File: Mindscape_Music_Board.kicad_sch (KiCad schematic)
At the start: 12 parts, among them J1 Conn_02x31_Row_Letter_First, SW1 SW_DIP_x08, U1 74LS08, U2 74LS74, U3 LM386, U4 74LS04, U5 74LS08, U6 74LS85, U7 74LS85, U8 AY-3-8913, U9 AY-3-8913

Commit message: More routing/footprints.
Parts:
- added C1, C11, C12, C2, C4, C5, C7, C99: C, Capacitor_THT:C_Disc_D7.5mm_W5.0mm_P7.50mm, symbol Device:C
- added C10: 470uF/16V, Capacitor_THT:CP_Axial_L18.0mm_D8.0mm_P25.00mm_Horizontal, symbol Device:C_Polarized
- added C14, C15: ?, Capacitor_THT:CP_Radial_Tantal_D4.5mm_P5.00mm, symbol Device:C_Polarized
- added C3, C8, C98: ?, Capacitor_THT:CP_Radial_D5.0mm_P2.50mm, symbol Device:C_Polarized
- added C6: C, Capacitor_THT:C_Disc_D3.0mm_W1.6mm_P2.50mm, symbol Device:C
- added J2: AudioJack2, MMB_Library:Audio_Jack, symbol Connector_Audio:AudioJack2
- added R1: 10, Resistor_THT:R_Axial_DIN0309_L9.0mm_D3.2mm_P12.70mm_Horizontal, symbol Device:R
- added R2, R3: ?, Resistor_THT:R_Axial_DIN0309_L9.0mm_D3.2mm_P12.70mm_Horizontal, symbol Device:R
- added RV1: 10K?, MMB_Library:Potentiometer, symbol Device:R_Potentiometer
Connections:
- net +12V: now also U3.6 (V+), C14.1, C6.1
- net AEN: now also U4.5
- net ANALOG: now also R2.1, R3.1
- net CLK: now also U2.2 (D), U2.6 (~{Q})
- net GND: now also C1.2, C11.2, C12.2, C14.2, C15.2, C2.2, C3.2, C4.2, C5.2, C6.2, C7.2, C98.2, C99.2, J2.S, R3.2, RV1.3; no longer J1.b10 (Pin_b10), J1.b31 (Pin_b31)
- net ISA_CLK: now also U2.3 (C)
- net VCC: now also C1.1, C11.1, C12.1, C15.1, C2.1, C4.1, C5.1
- net ~{IOR}: now also U1.13
- net ~{IOW}: now also U4.11
- net ~{RESET}: now also C98.1
- net BDIR1: now reaches U5.8
- net BDIR1: now also U9.2 (BDIR)
- net ~{AEN}: now reaches U4.6
- net ~{AEN}: now also U6.3 (Ia=b)
- net BC1_1: now reaches U9.3 (BC1)
- net BC1_1: now also U5.11
- net BDIR0: now reaches U8.2 (BDIR)
- net BDIR0: now also U5.6
- net BC1_0: now reaches U8.3 (BC1)
- net BC1_0: now also U5.3
- net at U7.2 (Ia<b): now also U6.7 (Oa<b)
- net at U7.3 (Ia=b): now also U6.6 (Oa=b)
- net ADDR_MATCH: now reaches U7.6 (Oa=b)
- net at U1.10: now also U1.5
- net at U3.3 (+): now also RV1.2
- net at U3.5: now also C10.1, R1.1
- new net: C99.1, R1.2
- new net: C8.2, RV1.1
- new net: C7.1, C8.1, R2.2
- new net: C10.2, J2.T
- no-connect marks 1 -> 7
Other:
- note added: "(CHIP1)"
- note added: "(DATA)"
- note added: "(~{CHIP1})"
- note added: "(~{DATA})"
- note added: "Function of this FF is an (un)educated guess"
- moved on the sheet: J1, RN1, SW1, U1A, U1B, U1C, U1D, U1E, U2B, U2C, U3, U4A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

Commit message: Worked out glue/decoding (hopefully).
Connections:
- net A1: now also U1.4
- net ADDR_MATCH: now also U1.10, U1.5
- net BC1_0: now also U5.11, U9.3 (BC1); no longer U5.3, U8.3 (BC1)
- net BC1_1: now also U5.3, U8.3 (BC1); no longer U5.11, U9.3 (BC1)
- net BDIR0: now also U5.8, U9.2 (BDIR); no longer U5.6, U8.2 (BDIR)
- net BDIR1: now also U5.6, U8.2 (BDIR); no longer U5.8, U9.2 (BDIR)
- net CHIP0: now also U1.9, U4.8
- net CONTROL: now also U1.1, U4.12
- net at U1.11: now also U4.1
- net at U1.12: now also U4.4
- net at U4.10, U5.10, U5.5: now also U1.2
- net at U5.9: now also U1.8, U5.12
- net at C3.1: now also U3.7 (BYPASS)
- net at U5.4: now also U1.6, U5.2
- net at U4.3: now also U1.3
- net ~{AEN}: no longer names the net of U4.6, U6.3 (Ia=b)
- no-connect marks 7 -> 9
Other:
- moved on the sheet: C3, J1, U1A, U1B, U1C, U1D, U1E, U2A, U2B, U2C, U4A, U4B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

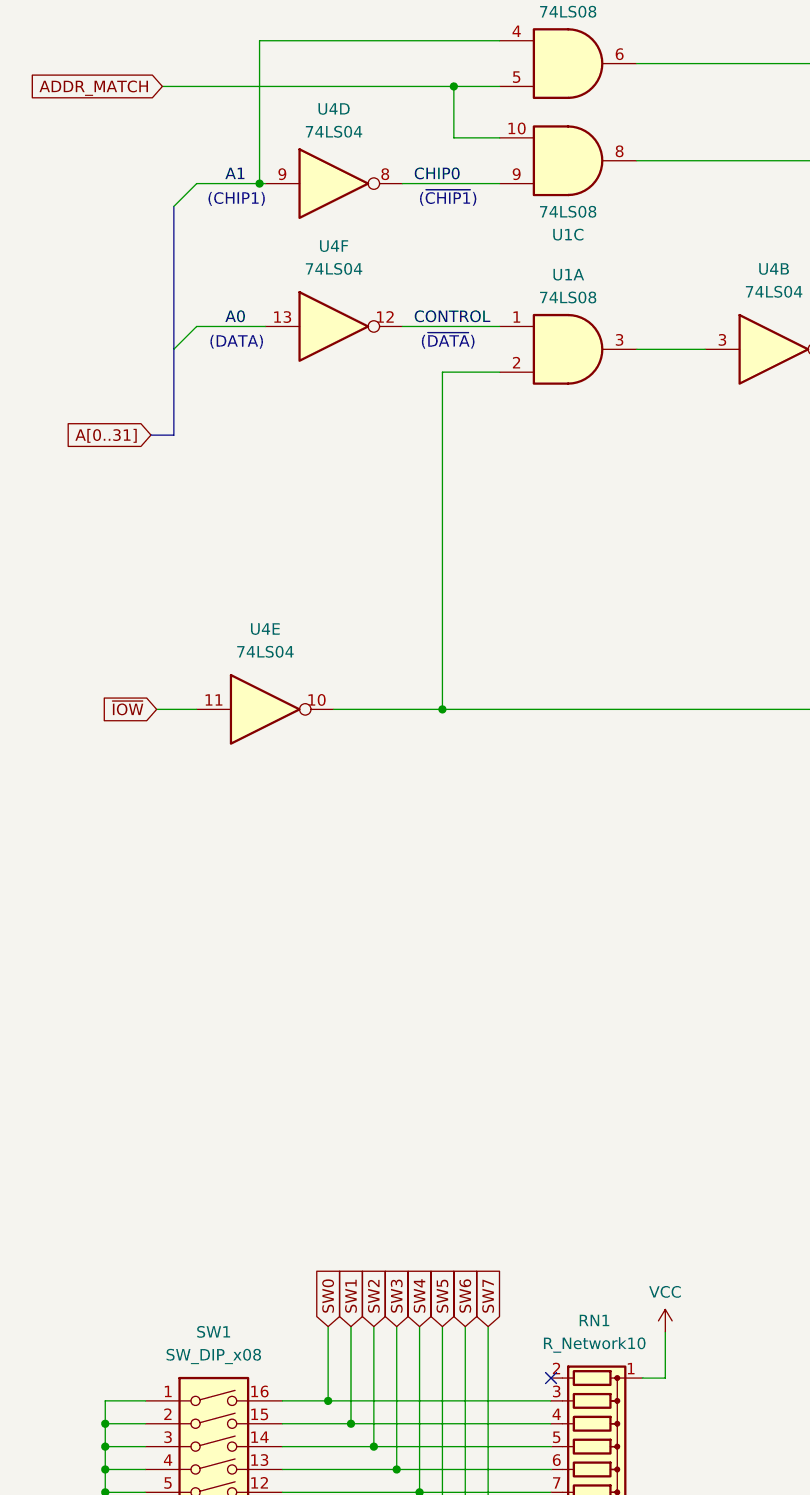
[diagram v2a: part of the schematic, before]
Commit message: Some more accurate footprints.
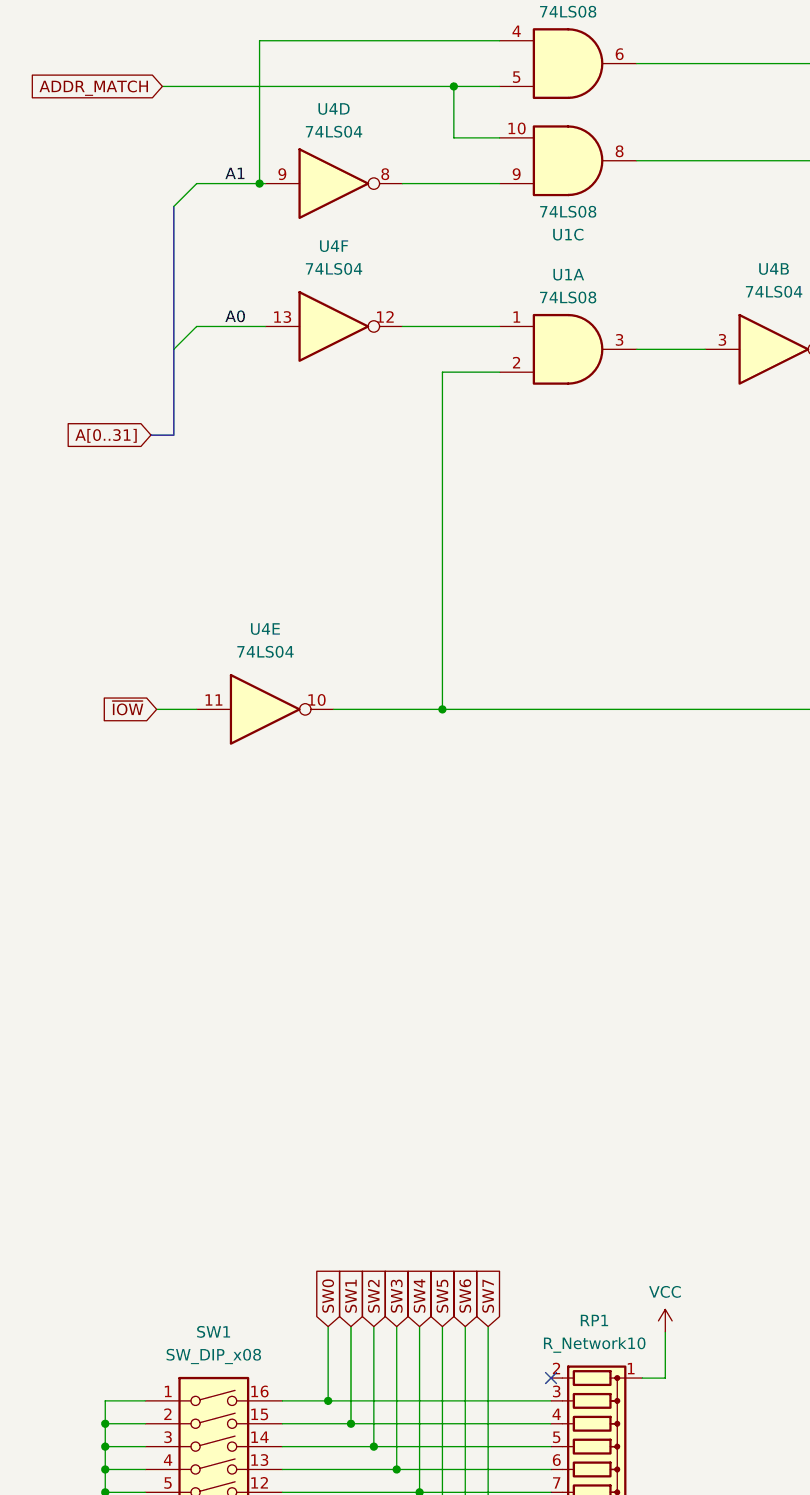
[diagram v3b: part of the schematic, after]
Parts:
- C1, C11, C12, C2, C4, C5: footprint Capacitor_THT:C_Disc_D7.5mm_W5.0mm_P7.50mm -> MMB_Library:C_Disc_P7.50mm
- C10: footprint Capacitor_THT:CP_Axial_L18.0mm_D8.0mm_P25.00mm_Horizontal -> MMB_Library:CP_Axial_P25.00mm_Horizontal
- C7, C99: footprint Capacitor_THT:C_Disc_D7.5mm_W5.0mm_P7.50mm -> MMB_Library:C_Poly_P7.50mm
- R1, R2, R3: footprint Resistor_THT:R_Axial_DIN0309_L9.0mm_D3.2mm_P12.70mm_Horizontal -> MMB_Library:R_P12.70mm
- renumbered RN1 to RP1
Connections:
- net CHIP0: no longer names the net of U1.9, U4.8
- net CONTROL: no longer names the net of U1.1, U4.12
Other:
- note removed: "(CHIP1)"
- note removed: "(DATA)"
- note removed: "(~{CHIP1})"
- note removed: "(~{DATA})"
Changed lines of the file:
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@@
 		)
 	)
-	(text "(~{CHIP1})"
-		(exclude_from_sim no)
-		(at 69.215 54.61 0)
-		(effects
-			(font
-				(size 1.27 1.27)
-			)
-		)
-	)
-	(text "(CHIP1)"
-		(exclude_from_sim no)
-		(at 45.72 54.61 0)
-		(effects
-			(font
-				(size 1.27 1.27)
-			)
-		)
-	)
-	(text "(DATA)"
-		(exclude_from_sim no)
-		(at 45.72 70.485 0)
-		(effects
-			(font
-				(size 1.27 1.27)
-			)
-		)
-	)
 	(text "Function of this FF is\nan (un)educated guess"
 		(exclude_from_sim no)
@@
 		)
 	)
-	(text "(~{DATA})"
-		(exclude_from_sim no)
-		(at 69.215 70.485 0)
-		(effects
-			(font
-				(size 1.27 1.27)
-			)
-		)
-	)
 	(label "A2"
 		(at 43.815 250.19 0)
@@
 		)
 	)
-	(label "CHIP0"
-		(at 65.405 52.705 0)
-		(effects
-			(font
-				(size 1.27 1.27)
-			)
-			(justify left bottom)
-		)
-	)
 	(label "A0"
 		(at 232.41 114.3 0)
@@
 		)
 	)
-	(label "CONTROL"
-		(at 65.405 68.58 0)
-		(effects
-			(font
-				(size 1.27 1.27)
-			)
-			(justify left bottom)
-		)
-	)
 	(global_label "BC1_0"
 		(shape input)
@@
 		(dnp no)
 		(fields_autoplaced yes)
-		(property "Reference" "RN1"
+		(property "Reference" "RP1"
 			(at 85.471 179.07 90)
 			(effects
@@
 			(project ""
 				(path "/d145a514-8ad3-4361-b45e-7dea21701e11"
-					(reference "RN1")
+					(reference "RP1")
 					(unit 1)
 				)
@@
 			)
 		)
-		(property "Footprint" "Capacitor_THT:C_Disc_D7.5mm_W5.0mm_P7.50mm"
+		(property "Footprint" "MMB_Library:C_Disc_P7.50mm"
 			(at 305.7652 212.725 0)
 			(effects
@@
 			)
 		)
-		(property "Footprint" "Resistor_THT:R_Axial_DIN0309_L9.0mm_D3.2mm_P12.70mm_Horizontal"
+		(property "Footprint" "MMB_Library:R_P12.70mm"
 			(at 356.997 157.48 90)
 			(effects
@@
 			)
 		)
-		(property "Footprint" "Capacitor_THT:C_Disc_D7.5mm_W5.0mm_P7.50mm"
+		(property "Footprint" "MMB_Library:C_Disc_P7.50mm"
 			(at 317.1952 212.725 0)
 			(effects
@@
 			)
 		)
-		(property "Footprint" "Capacitor_THT:C_Disc_D7.5mm_W5.0mm_P7.50mm"
+		(property "Footprint" "MMB_Library:C_Disc_P7.50mm"
 			(at 294.3352 212.725 0)
 			(effects
@@
 			)
 		)
-		(property "Footprint" "Resistor_THT:R_Axial_DIN0309_L9.0mm_D3.2mm_P12.70mm_Horizontal"
+		(property "Footprint" "MMB_Library:R_P12.70mm"
 			(at 282.067 140.335 90)
 			(effects
@@
 			)
 		)
-		(property "Footprint" "Capacitor_THT:C_Disc_D7.5mm_W5.0mm_P7.50mm"
+		(property "Footprint" "MMB_Library:C_Disc_P7.50mm"
 			(at 282.9052 212.725 0)
 			(effects
@@
 			)
 		)
-		(property "Footprint" "Capacitor_THT:C_Disc_D7.5mm_W5.0mm_P7.50mm"
+		(property "Footprint" "MMB_Library:C_Disc_P7.50mm"
 			(at 327.9902 212.725 0)
 			(effects
@@
 			)
 		)
-		(property "Footprint" "Capacitor_THT:C_Disc_D7.5mm_W5.0mm_P7.50mm"
+		(property "Footprint" "MMB_Library:C_Poly_P7.50mm"
 			(at 300.6598 143.51 0)
 			(effects
@@
 			)
 		)
-		(property "Footprint" "Resistor_THT:R_Axial_DIN0309_L9.0mm_D3.2mm_P12.70mm_Horizontal"
+		(property "Footprint" "MMB_Library:R_P12.70mm"
 			(at 292.735 135.128 90)
 			(effects
@@
 			)
 		)
-		(property "Footprint" "Capacitor_THT:CP_Axial_L18.0mm_D8.0mm_P25.00mm_Horizontal"
+		(property "Footprint" "MMB_Library:CP_Axial_P25.00mm_Horizontal"
 			(at 372.11 148.2598 0)
 			(effects
@@
 			)
 		)
-		(property "Footprint" "Capacitor_THT:C_Disc_D7.5mm_W5.0mm_P7.50mm"
+		(property "Footprint" "MMB_Library:C_Poly_P7.50mm"
 			(at 359.7402 172.72 0)
 			(effects
@@
 			)
 		)
-		(property "Footprint" "Capacitor_THT:C_Disc_D7.5mm_W5.0mm_P7.50mm"
+		(property "Footprint" "MMB_Library:C_Disc_P7.50mm"
 			(at 271.4752 212.725 0)
 			(effects

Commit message: Footprints/silkscreen
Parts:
- C13: renamed from C98; footprint Capacitor_THT:CP_Radial_D5.0mm_P2.50mm -> MMB_Library:CP_Radial_P2.50mm
- C14, C15: footprint Capacitor_THT:CP_Radial_Tantal_D4.5mm_P5.00mm -> MMB_Library:CP_Radial_P5.00mm
- C3, C8: footprint Capacitor_THT:CP_Radial_D5.0mm_P2.50mm -> MMB_Library:CP_Radial_P2.50mm
- C6: footprint Capacitor_THT:C_Disc_D3.0mm_W1.6mm_P2.50mm -> MMB_Library:CP_Radial_P2.50mm
- R2: value ? -> 220
- R3: value ? -> 1K
- SW1: footprint Button_Switch_THT:SW_DIP_SPSTx08_Slide_6.7x21.88mm_W7.62mm_P2.54mm_LowProfile -> MMB_Library:SW_DIP_SPSTx08
- U8, U9: footprint Package_DIP:DIP-24_18.0mmx34.29mm_W15.24mm -> MMB_Library:DIP-24
- renumbered C99 to C9, RV1 to R4
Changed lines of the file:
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@@
 			)
 		)
-		(property "Footprint" "Capacitor_THT:CP_Radial_Tantal_D4.5mm_P5.00mm"
+		(property "Footprint" "MMB_Library:CP_Radial_P5.00mm"
 			(at 378.1552 215.265 0)
 			(effects
@@
 			)
 		)
-		(property "Footprint" "Capacitor_THT:CP_Radial_D5.0mm_P2.50mm"
+		(property "Footprint" "MMB_Library:CP_Radial_P2.50mm"
 			(at 358.4702 127.635 0)
 			(effects
@@
 			)
 		)
-		(property "Footprint" "Package_DIP:DIP-24_18.0mmx34.29mm_W15.24mm"
+		(property "Footprint" "MMB_Library:DIP-24"
 			(at 232.41 146.05 0)
 			(effects
@@
 			)
 		)
-		(property "Footprint" "Package_DIP:DIP-24_18.0mmx34.29mm_W15.24mm"
+		(property "Footprint" "MMB_Library:DIP-24"
 			(at 160.02 146.05 0)
 			(effects
@@
 			)
 		)
-		(property "Footprint" "Capacitor_THT:CP_Radial_Tantal_D4.5mm_P5.00mm"
+		(property "Footprint" "MMB_Library:CP_Radial_P5.00mm"
 			(at 341.3252 212.725 0)
 			(effects
@@
 		(dnp no)
 		(fields_autoplaced yes)
-		(property "Reference" "RV1"
+		(property "Reference" "R4"
 			(at 321.31 145.4149 0)
 			(effects
@@
 			(project ""
 				(path "/d145a514-8ad3-4361-b45e-7dea21701e11"
-					(reference "RV1")
+					(reference "R4")
 					(unit 1)
 				)
@@
 			)
 		)
-		(property "Footprint" "Capacitor_THT:CP_Radial_D5.0mm_P2.50mm"
+		(property "Footprint" "MMB_Library:CP_Radial_P2.50mm"
 			(at 316.865 134.3152 0)
 			(effects
@@
 		(fields_autoplaced yes)
 		(property "Reference" "R3"
-			(at 286.385 139.0649 0)
+			(at 285.75 139.0649 0)
 			(effects
 				(font
@@
 			)
 		)
-		(property "Value" "?"
-			(at 286.385 141.6049 0)
+		(property "Value" "1K"
+			(at 285.75 141.6049 0)
 			(effects
 				(font
@@
 			)
 		)
-		(property "Footprint" "Capacitor_THT:C_Disc_D3.0mm_W1.6mm_P2.50mm"
+		(property "Footprint" "MMB_Library:CP_Radial_P2.50mm"
 			(at 366.0902 215.265 0)
 			(effects
@@
 			)
 		)
-		(property "Footprint" "Button_Switch_THT:SW_DIP_SPSTx08_Slide_6.7x21.88mm_W7.62mm_P2.54mm_LowProfile"
+		(property "Footprint" "MMB_Library:SW_DIP_SPSTx08"
 			(at 43.18 198.12 0)
 			(effects
@@
 		(fields_autoplaced yes)
 		(property "Reference" "R2"
-			(at 292.735 127.635 90)
+			(at 292.735 127 90)
 			(effects
 				(font
@@
 			)
 		)
-		(property "Value" "?"
-			(at 292.735 130.175 90)
+		(property "Value" "220"
+			(at 292.735 129.54 90)
 			(effects
 				(font
@@
 		(dnp no)
 		(fields_autoplaced yes)
-		(property "Reference" "C99"
-			(at 362.585 167.6399 0)
+		(property "Reference" "C9"
+			(at 361.95 167.6399 0)
 			(effects
 				(font
@@
 		)
 		(property "Value" "C"
-			(at 362.585 170.1799 0)
+			(at 361.95 170.1799 0)
 			(effects
 				(font
@@
 			(project ""
 				(path "/d145a514-8ad3-4361-b45e-7dea21701e11"
-					(reference "C99")
+					(reference "C9")
 					(unit 1)
 				)
@@
 		(dnp no)
 		(fields_autoplaced yes)
-		(property "Reference" "C98"
-			(at 290.195 235.9659 0)
+		(property "Reference" "C13"
+			(at 290.83 235.9659 0)
 			(effects
 				(font
@@
 		)
 		(property "Value" "?"
-			(at 290.195 238.5059 0)
+			(at 290.83 238.5059 0)
 			(effects
 				(font
@@
 			)
 		)
-		(property "Footprint" "Capacitor_THT:CP_Radial_D5.0mm_P2.50mm"
+		(property "Footprint" "MMB_Library:CP_Radial_P2.50mm"
 			(at 287.9852 241.935 0)
 			(effects
@@
 			(project "Mindscape_Music_Board"
 				(path "/d145a514-8ad3-4361-b45e-7dea21701e11"
-					(reference "C98")
+					(reference "C13")
 					(unit 1)
 				)

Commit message: Added notes to schematic.
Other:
- note added: "Bit odd that only one ground pin is connected, there are more but given the size of the card one might just be enough."
- note added: "Chip selects don't seem to go anywhere... they are pulled low internally so presumably BDIR and BC1 are enough."
- note added: "DIP switch selects base address but the software appears to use 300h hard-coded, so set the first two switches."
- note added: "Decoding is not done in full, A0 is ignored for reading. Reading with A0=0 would suggest reading the address latch, which makes little sense and would be a no-op anyway. So any reads just read the actual PSG data as if A0=1."
- note added: "Doesn't look like anything on the ISA bus is used for reset. The AY chips' resets have internal pull-ups so maybe this cap is just enough for power on."
- note added: "Function of this FF is an (un)educated guess... frequency divider such that CLK is half the frequency of ISA_CLK. That would make CLK 4.77/2 = 2.385 MHz which is below the 2.5 MHz maximum."
- note added: "It doesn't look like the second FF is used but it's feasible that ISA_CLK may be halved again. Board layout/traces do not suggest this however. Unused inputs should probably be tied to something, can't see if this was done on the original board."
- note added: "This circuit is pretty much straight out of the datasheet. Taking a guess that C3 is connected to the bypass pin."
- note removed: "Function of this FF is an (un)educated guess"
- moved on the sheet: C1, C11, C12, C13, C14, C15, C2, C4, C5, C6, U2B, U8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

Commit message: Tidying, BOM, annotations.
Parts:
- C1, C11, C4, C5: value C -> ~100nF; now not fitted
- C12, C2: value C -> ~100nF
- C13, C3, C8: value ? -> 10uF/16V?
- C14, C15: value ? -> 10uF/16V?; now not fitted
- C6: value C -> ~100nF?
- C7, C9: value C -> 47nF
- J1: value Conn_02x31_Row_Letter_First -> ISA
- RP1: value R_Network10 -> 4.7-10K
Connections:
- no-connect marks 9 -> 13
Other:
- note added: "C6 is marked as polarised but looks the same as the rest of the original decoupling caps."
- note added: "Most decoupling caps are not populated on the original board but you might want to add them."
- moved on the sheet: C12, C2, C6, RP1, SW1, U1E, U2C, U4C, U4G, U5E, U6, U7

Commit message: Minor schematic/PCB tweaks.
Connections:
- net SW0: now also RP1.10 (R9), SW1.9, U6.9 (B0); no longer RP1.3 (R2), SW1.16, U7.1 (B3)
- net SW1: now also RP1.9 (R8), SW1.10, U6.11 (B1); no longer RP1.4 (R3), SW1.15, U7.14 (B2)
- net SW2: now also RP1.8 (R7), SW1.11, U6.14 (B2); no longer RP1.5 (R4), SW1.14, U7.11 (B1)
- net SW3: now also RP1.7 (R6), SW1.12, U6.1 (B3); no longer RP1.6 (R5), SW1.13, U7.9 (B0)
- net SW4: now also RP1.6 (R5), SW1.13, U7.9 (B0); no longer RP1.7 (R6), SW1.12, U6.1 (B3)
- net SW5: now also RP1.5 (R4), SW1.14, U7.11 (B1); no longer RP1.8 (R7), SW1.11, U6.14 (B2)
- net SW6: now also RP1.4 (R3), SW1.15, U7.14 (B2); no longer RP1.9 (R8), SW1.10, U6.11 (B1)
- net SW7: now also RP1.3 (R2), SW1.16, U7.1 (B3); no longer RP1.10 (R9), SW1.9, U6.9 (B0)
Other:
- note added: "DIP switch selects base address but the software appears to use 300h hard-coded, so set the first two switches, i.e. close all except 1 (SW7) and 2 (SW6)."
- note removed: "DIP switch selects base address but the software appears to use 300h hard-coded, so set the first two switches."
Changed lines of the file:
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@@
 		)
 	)
-	(text "DIP switch selects base address but the\nsoftware appears to use 300h hard-coded,\nso set the first two switches."
+	(text "DIP switch selects base address but the\nsoftware appears to use 300h hard-coded,\nso set the first two switches, i.e.\nclose all except 1 (SW7) and 2 (SW6)."
 		(exclude_from_sim no)
-		(at 43.18 154.94 0)
+		(at 43.18 153.67 0)
 		(effects
 			(font
@@
 	)
 	(label "SW3"
-		(at 111.76 237.49 0)
+		(at 36.83 229.87 0)
 		(effects
 			(font
@@
 	)
 	(label "SW0"
-		(at 111.76 229.87 0)
+		(at 36.83 237.49 0)
 		(effects
 			(font
@@
 	)
 	(label "SW5"
-		(at 36.195 232.41 0)
+		(at 111.76 234.95 0)
 		(effects
 			(font
@@
 	)
 	(label "A6"
-		(at 234.315 99.06 180)
+		(at 234.95 99.06 180)
 		(effects
 			(font
@@
 	)
 	(label "SW4"
-		(at 66.04 170.815 90)
+		(at 63.5 170.815 90)
 		(effects
 			(font
@@
 	)
 	(label "SW1"
-		(at 58.42 170.815 90)
+		(at 71.12 170.815 90)
 		(effects
 			(font
@@
 	)
 	(label "SW2"
-		(at 60.96 170.815 90)
+		(at 68.58 170.815 90)
 		(effects
 			(font
@@
 	)
 	(label "SW6"
-		(at 71.12 170.815 90)
+		(at 58.42 170.815 90)
 		(effects
 			(font
@@
 	)
 	(label "SW4"
-		(at 36.195 229.87 0)
+		(at 111.76 237.49 0)
 		(effects
 			(font
@@
 	)
 	(label "SW6"
-		(at 36.195 234.95 0)
+		(at 111.76 232.41 0)
 		(effects
 			(font
@@
 	)
 	(label "SW7"
-		(at 73.66 170.815 90)
+		(at 55.88 170.815 90)
 		(effects
 			(font
@@
 	)
 	(label "A9"
-		(at 234.315 91.44 180)
+		(at 234.95 91.44 180)
 		(effects
 			(font
@@
 	)
 	(label "SW3"
-		(at 63.5 170.815 90)
+		(at 66.04 170.815 90)
 		(effects
 			(font
@@
 	)
 	(label "SW7"
-		(at 36.195 237.49 0)
+		(at 111.76 229.87 0)
 		(effects
 			(font
@@
 	)
 	(label "SW2"
-		(at 111.76 234.95 0)
+		(at 36.83 232.41 0)
 		(effects
 			(font
@@
 	)
 	(label "SW5"
-		(at 68.58 170.815 90)
+		(at 60.96 170.815 90)
 		(effects
 			(font
@@
 	)
 	(label "SW0"
-		(at 55.88 170.815 90)
+		(at 73.66 170.815 90)
 		(effects
 			(font
@@
 	)
 	(label "A7"
-		(at 234.315 96.52 180)
+		(at 234.95 96.52 180)
 		(effects
 			(font
@@
 	)
 	(label "SW1"
-		(at 111.76 232.41 0)
+		(at 36.83 234.95 0)
 		(effects
 			(font
@@
 	)
 	(label "A8"
-		(at 234.315 93.98 180)
-		(effects
-			(font
+		(at 234.95 93.98 180)
+		(effects
+			(font
